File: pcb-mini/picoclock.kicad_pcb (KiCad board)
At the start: 4 copper layers, 140 x 54 mm, 144 parts, among them J1 UART, J10 USB, J11 ESP32_UART1, J12 LED_5V, J13 ESP32_IO0, J14 SJ2-35863B1-SMT-TR, J15 Conn_01x24, J16 UART_S88, J2 USB_A, J3 UART, J4 xx, J5 Micro_SD_Card_Det1, J6 USB_C_Receptacle, J7 DBG, J8 Conn_01x21_Pin, J9 AUDIO, Q1 BSS138, Q3 BSS138, SW1 SW_Push, SW2 SW_Push, SW3 SW_Push, SW4 SW_Push, SW5 SW_Push, SW6 SW_Push, SW7 SW_Push, U1 PCF8563T, U10 74LS157, U12 ENS160, U13 TCR2EE19, U15 SHT4x, U2 RP2350_80QFN, U3 MCP9808_MSOP, U4 PCM5100, U5 PAM8302A, U6 W25Q128JVS, U7 MCP45X1-104E, U8 NCP1117-3.3_SOT223, U9 ESP32-WROOM-E, Y1 Crystal, Y2 ABM8-272-T3

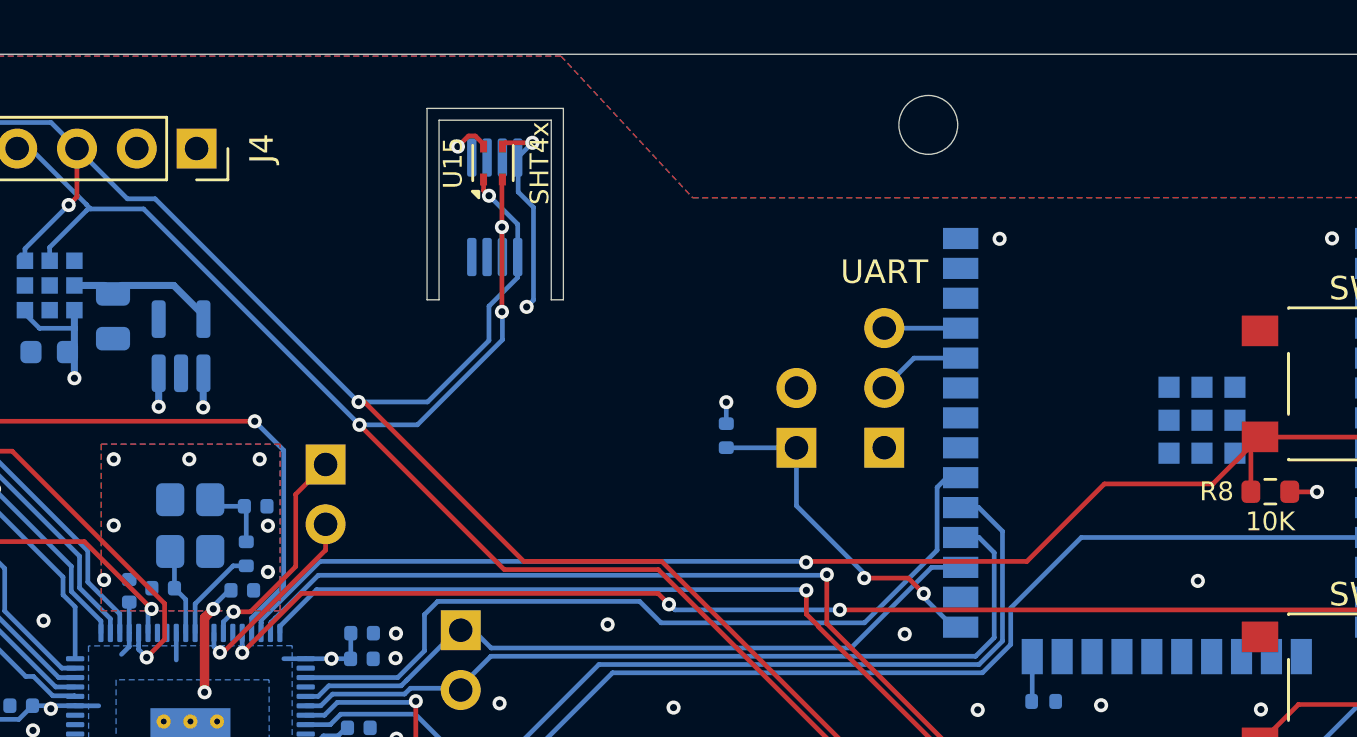
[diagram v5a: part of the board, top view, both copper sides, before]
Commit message: [pcb] mini: add STCC4 and SCD41
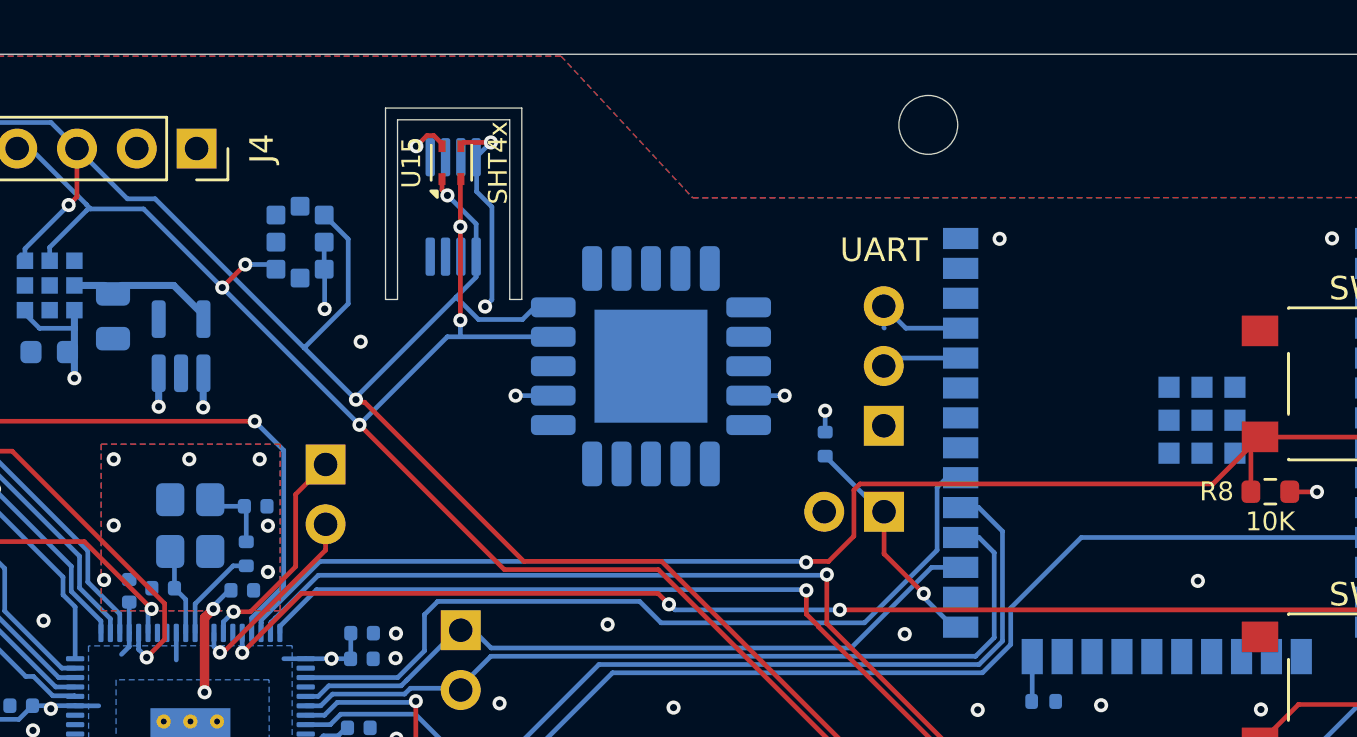
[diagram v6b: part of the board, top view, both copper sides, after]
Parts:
- added U16: SCD41-D-R2, Sensor:Sensirion_SCD4x-1EP_10.1x10.1mm_P1.25mm_EP4.8x4.8mm, B.Cu at (169.4, 93.2)
- added U17: STCC4, stcc4:STCC4, B.Cu at (154.5, 88.0)
- moved J13 4.61 mm to (179.3, 99.4), turned to 90 degrees
- moved R31 4.22 mm to (176.8, 96.6)
- moved U15 1.77 mm to (160.9, 84.6)
- moved U3 1.77 mm to (161.0, 86.5)
- moved J3 0.93 mm to (179.3, 95.8)
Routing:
- net SDA: track 132.3 -> 141.3 mm
- net +3V3: track 113.5 -> 119.5 mm, vias 40 -> 43
- net SCL: track 123.8 -> 128.7 mm, vias 4 -> 6
- net ESP32_IO0: track 14.8 -> 9.91 mm, vias 2 -> 1
- net GPIO8/btn: track 58.1 -> 59.3 mm
- net GND: vias 129 -> 130
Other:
- outline, holes or cut-outs redrawn
